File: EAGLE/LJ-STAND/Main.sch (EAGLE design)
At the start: 119 parts

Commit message: TSOP wires routed. Sanity gone.
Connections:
- removed net N$22: SW1.6
- net +3V3: now also BLUETOOTH.2
- net DIP3: now also SW1.6
- net GND: now also BLUETOOTH.3
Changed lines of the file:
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@@
 </segment>
 <segment>
-<wire x1="132.08" y1="182.88" x2="144.78" y2="182.88" width="0.1524" layer="91"/>
 <wire x1="144.78" y1="182.88" x2="144.78" y2="180.34" width="0.1524" layer="91"/>
 <pinref part="GND93" gate="1" pin="GND"/>
+<pinref part="BLUETOOTH" gate="G$1" pin="3"/>
+<wire x1="132.08" y1="182.88" x2="144.78" y2="182.88" width="0.1524" layer="91"/>
 </segment>
 <segment>
@@
 </segment>
 <segment>
-<wire x1="132.08" y1="180.34" x2="134.62" y2="180.34" width="0.1524" layer="91"/>
 <wire x1="134.62" y1="180.34" x2="134.62" y2="175.26" width="0.1524" layer="91"/>
 <wire x1="134.62" y1="175.26" x2="139.7" y2="175.26" width="0.1524" layer="91"/>
 <wire x1="139.7" y1="175.26" x2="139.7" y2="177.8" width="0.1524" layer="91"/>
 <pinref part="+3V21" gate="G$1" pin="+3V3"/>
+<pinref part="BLUETOOTH" gate="G$1" pin="2"/>
+<wire x1="132.08" y1="180.34" x2="134.62" y2="180.34" width="0.1524" layer="91"/>
 </segment>
 <segment>
@@
 </segment>
 </net>
-<net name="N$22" class="0">
-<segment>
-<pinref part="SW1" gate="A" pin="6"/>
-<wire x1="170.18" y1="116.84" x2="195.58" y2="116.84" width="0.1524" layer="91"/>
-</segment>
-</net>
 <net name="DIP2" class="0">
 <segment>
@@
 <net name="DIP3" class="0">
 <segment>
-<wire x1="195.58" y1="116.84" x2="195.58" y2="119.38" width="0.1524" layer="91"/>
-<wire x1="195.58" y1="116.84" x2="200.66" y2="116.84" width="0.1524" layer="91"/>
 <wire x1="200.66" y1="116.84" x2="200.66" y2="132.08" width="0.1524" layer="91"/>
 <label x="200.66" y="132.08" size="1.778" layer="95" rot="R90" xref="yes"/>
+<pinref part="SW1" gate="A" pin="6"/>
+<wire x1="200.66" y1="116.84" x2="195.58" y2="116.84" width="0.1524" layer="91"/>
+<pinref part="R11" gate="G$1" pin="1"/>
+<wire x1="195.58" y1="116.84" x2="170.18" y2="116.84" width="0.1524" layer="91"/>
+<wire x1="195.58" y1="119.38" x2="195.58" y2="116.84" width="0.1524" layer="91"/>
 <junction x="195.58" y="116.84"/>
-<pinref part="R11" gate="G$1" pin="1"/>
-</segment>
-<segment>
+</segment>
+<segment>

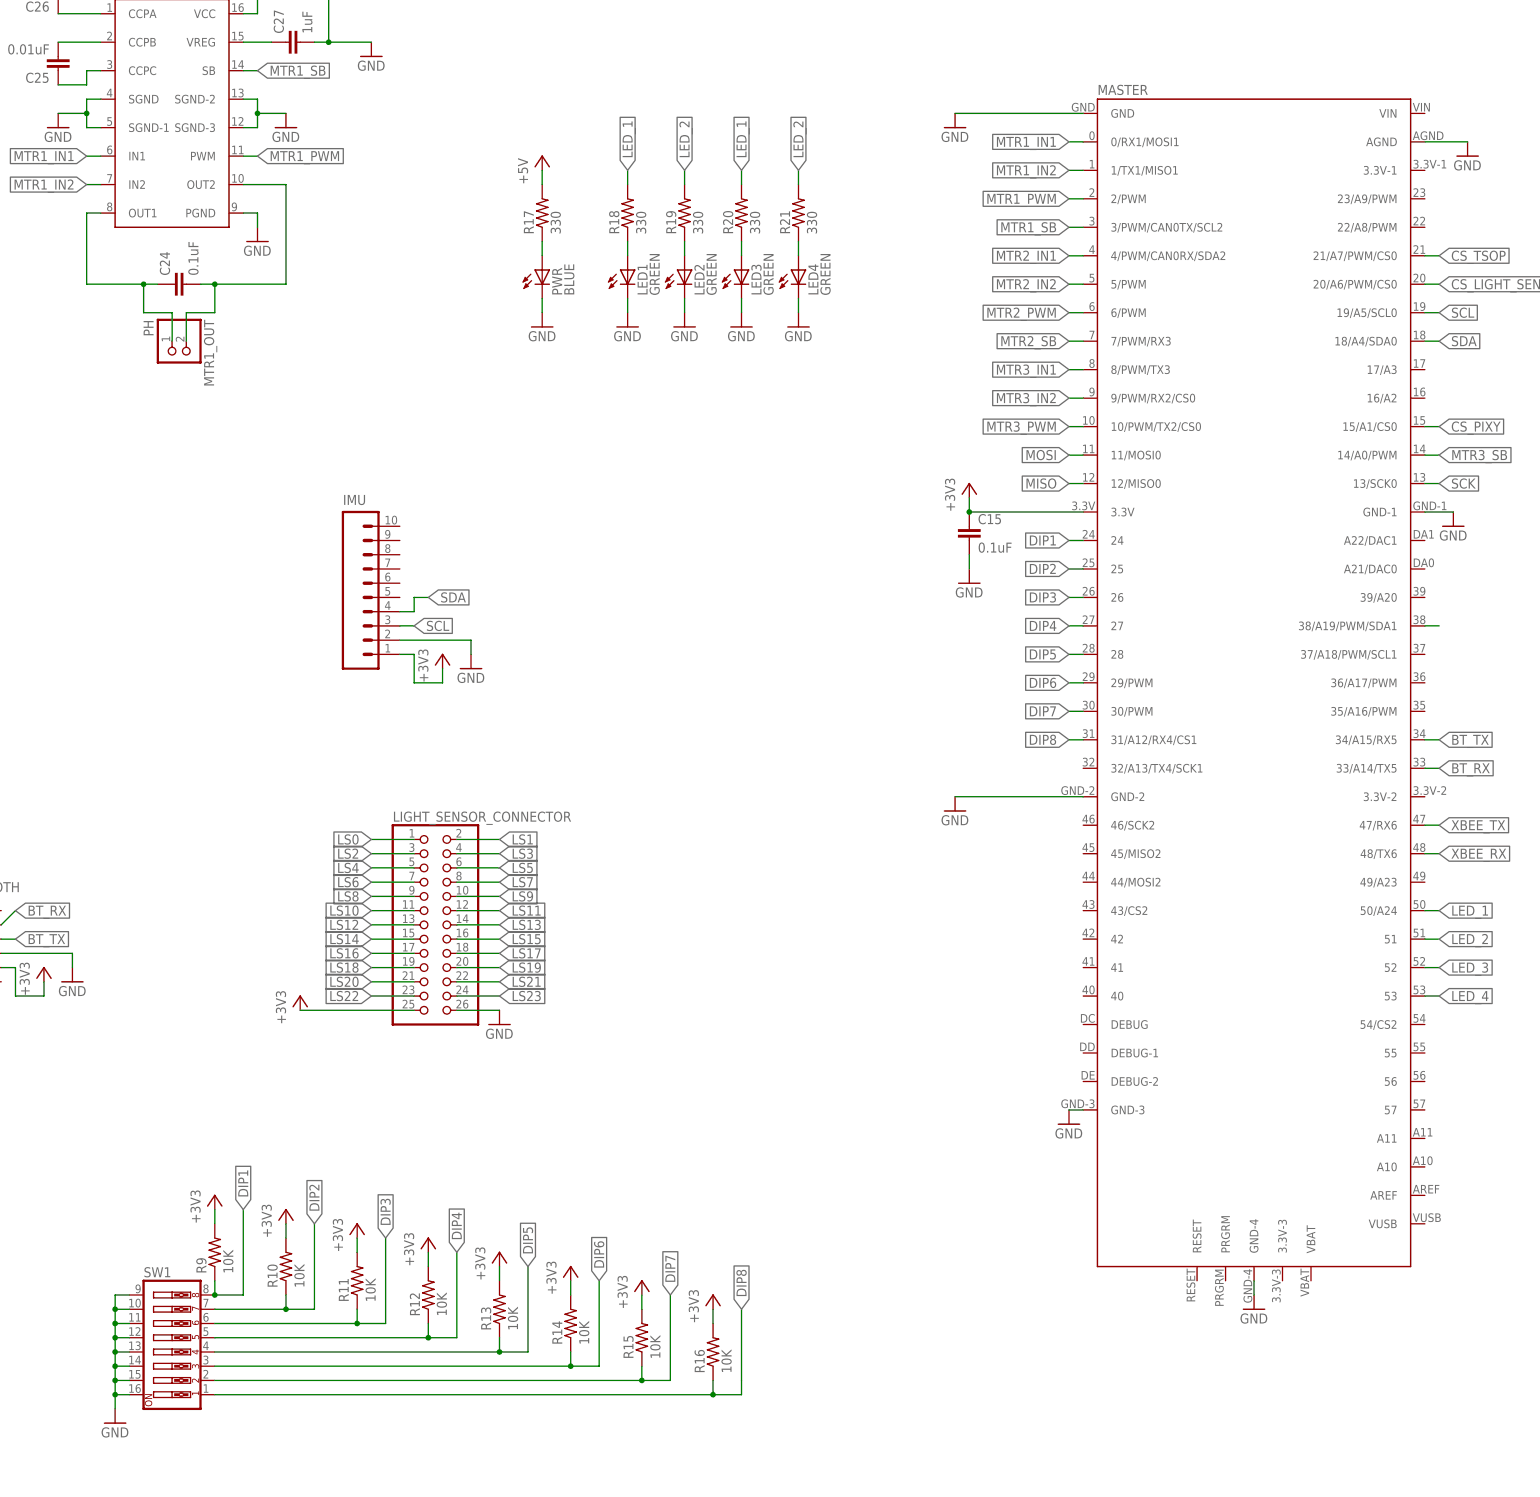
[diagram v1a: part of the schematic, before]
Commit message: Finished main PCB routing
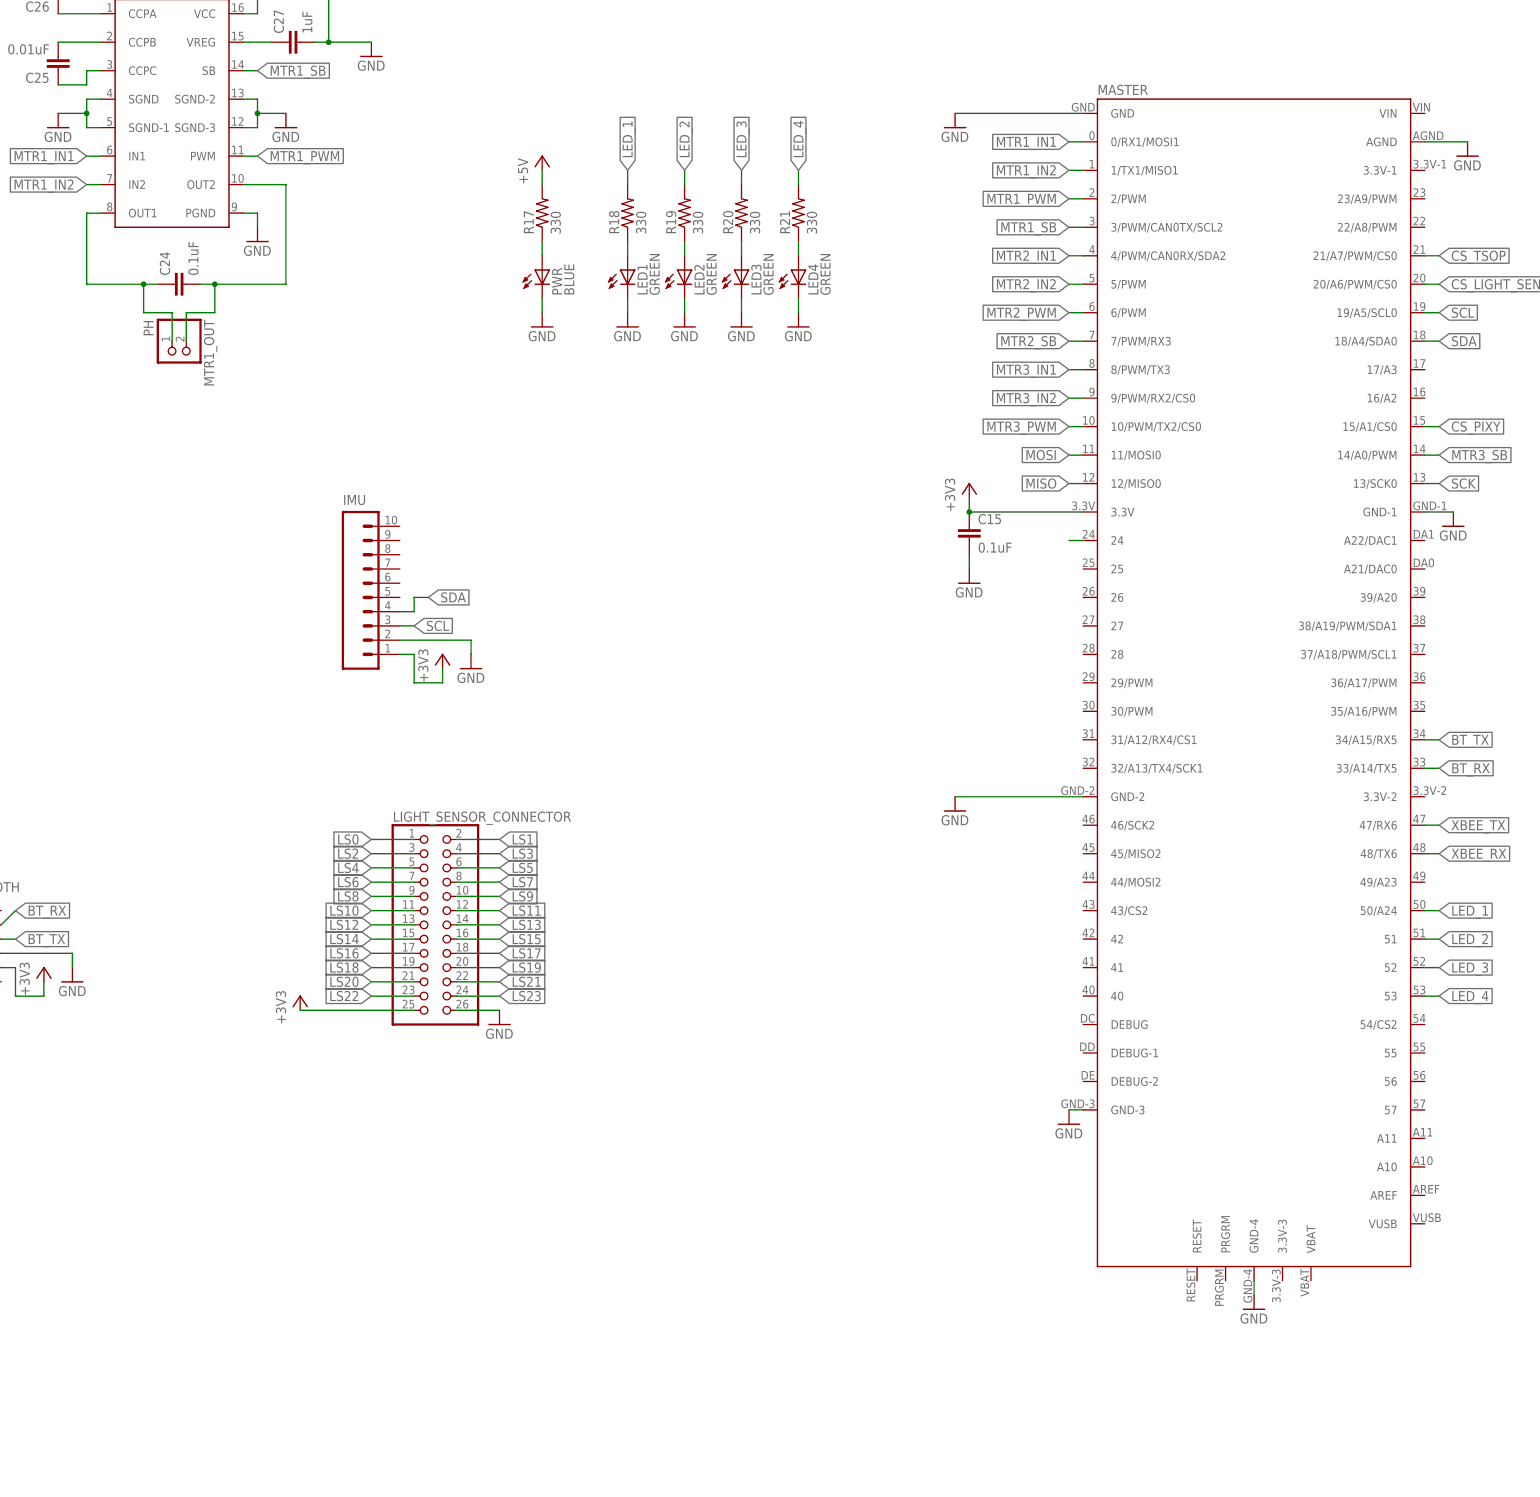
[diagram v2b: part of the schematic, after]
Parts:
- removed R10, R11, R12, R13, R14, R15, R16, R9: 10K, SparkFun-Resistors:RESISTOR0603-RES
- removed SW1: (no value), SparkFun-Electromechanical:SW_DIP-8
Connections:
- removed net DIP2: MASTER.25, R10.1, SW1.7
- removed net DIP3: MASTER.26, R11.1, SW1.6
- removed net DIP4: MASTER.27, R12.1, SW1.5
- removed net DIP5: MASTER.28, R13.1, SW1.4
- removed net DIP6: MASTER.29/PWM, R14.1, SW1.3
- removed net DIP7: MASTER.30/PWM, R15.1, SW1.2
- removed net DIP8: MASTER.31/A12/RX4/CS1, R16.1, SW1.1
- net +3V3: no longer R10.2, R11.2, R12.2, R13.2, R14.2, R15.2, R16.2, R9.2
- net DIP1: no longer R9.1, SW1.8
- net GND: no longer SW1.10, SW1.11, SW1.12, SW1.13, SW1.14, SW1.15, SW1.16, SW1.9
- net LED_1: no longer R20.2
- net LED_2: no longer R21.2
- net LED_3: now also R20.2
- net LED_4: now also R21.2
- net SDA: no longer MASTER.38/A19/PWM/SDA1

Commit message: Teensys
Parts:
- added C48: 100uF, SparkFun-Capacitors:CAP_POLPTH1
- added C49: 0.1uF, SparkFun-Capacitors:CAP0603-CAP
- added C50: 0.01uF, SparkFun-Capacitors:CAP0603-CAP
- added C51: 0.22uF, SparkFun-Capacitors:CAP0603-CAP
- added C52: 1uF, SparkFun-Capacitors:CAP0603-CAP
- added MOTOR_4: TB6549PG, TB6549PG-motor-controller:TB6549PG
- added MTR4_OUT: PH, adafruit:JST_2PIN-SMT
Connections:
- removed net DIP1: MASTER.24
- new net MTR4_IN1: MASTER.17/A3, MOTOR_4.IN1
- new net MTR4_IN2: MASTER.22/A8/PWM, MOTOR_4.IN2
- new net MTR4_PWM: MASTER.23/A9/PWM, MOTOR_4.PWM
- new net MTR4_SB: MASTER.24, MOTOR_4.SB
- new net N$22: C49.1, MOTOR_4.OUT1, MTR4_OUT.2
- new net N$26: C49.2, MOTOR_4.OUT2, MTR4_OUT.1
- new net N$28: C50.2, MOTOR_4.CCPB
- new net N$30: C50.1, MOTOR_4.CCPC
- new net N$31: C51.1, MOTOR_4.CCPA
- new net N$32: C52.1, MOTOR_4.VREG
- net GND: now also C48.-, C51.2, C52.2, MOTOR_4.PGND, MOTOR_4.SGND, MOTOR_4.SGND-1, MOTOR_4.SGND-2, MOTOR_4.SGND-3
- net LED_1: now also MASTER.38/A19/PWM/SDA1; no longer MASTER.50/A24
- net LED_2: now also MASTER.37/A18/PWM/SCL1; no longer MASTER.51
- net LED_3: now also MASTER.36/A17/PWM; no longer MASTER.52
- net LED_4: now also MASTER.35/A16/PWM; no longer MASTER.53
- net MOTOR_PWR: now also C48.+, MOTOR_4.VCC
- net MTR3_SB: now also MASTER.16/A2; no longer MASTER.14/A0/PWM
- net SCK: now also MASTER.14/A0/PWM; no longer MASTER.13/SCK0
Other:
- moved on the sheet: BLUETOOTH, C15, PIXY_I2C, PIXY_SPI, R1, R2, R5, R6, R7, R8, SCL, SDA

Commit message: Light sensor connector
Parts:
- added LED5: WHITE, adafruit:LEDCHIPLED_0603
- added LED6: YELLOW, adafruit:LEDCHIPLED_0603
- added R3, R4: 330, SparkFun-Resistors:RESISTOR0603
- LED2: value GREEN -> ORANGE
- LED3: value GREEN -> PINK
- LED4: value GREEN -> RED
- renumbered MTR1_OUT to MTR1_OUT_RIGHT, MTR2_OUT to MTR2_OUT_LEFT, MTR3_OUT to MTR3_OUT_BACKRIGHT, MTR4_OUT to MTR4_OUT_BACKLEFT
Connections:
- net LED_1 renamed LED1
- net LED_2 renamed LED2
- net LED_3 renamed LED3
- net LED_4 renamed LED4
- removed net CS_LIGHT_SENSOR: MASTER.20/A6/PWM/CS0, SLAVE_LIGHT.10/PWM/TX2/CS0
- new net CS_LIGHT: MASTER.9/PWM/RX2/CS0, SLAVE_LIGHT.10/PWM/TX2/CS0
- new net LED5: MASTER.29/PWM, R3.2
- new net LED6: MASTER.30/PWM, R4.2
- new net N$33: LED5.A, R3.1
- new net N$34: LED6.A, R4.1
- net CS_TSOP: now also MASTER.10/PWM/TX2/CS0, SLAVE_TSOP.10/PWM/TX2/CS0; no longer MASTER.21/A7/PWM/CS0, SLAVE_TSOP.15/A1/CS0
- net GND: now also LED5.C, LED6.C
- net LS0: now also SLAVE_LIGHT.15/A1/CS0; no longer SLAVE_LIGHT.14/A0/PWM
- net LS1: now also SLAVE_LIGHT.16/A2; no longer SLAVE_LIGHT.15/A1/CS0
- net LS10: now also SLAVE_LIGHT.A11; no longer SLAVE_LIGHT.A10
- net LS11: now also SLAVE_LIGHT.31/A12/RX4/CS1; no longer SLAVE_LIGHT.A11
- net LS12: now also SLAVE_LIGHT.32/A13/TX4/SCK1; no longer SLAVE_LIGHT.31/A12/RX4/CS1
- net LS13: now also SLAVE_LIGHT.33/A14/TX5; no longer SLAVE_LIGHT.32/A13/TX4/SCK1
- net LS14: now also SLAVE_LIGHT.34/A15/RX5; no longer SLAVE_LIGHT.33/A14/TX5
- net LS15: now also SLAVE_LIGHT.35/A16/PWM; no longer SLAVE_LIGHT.34/A15/RX5
- net LS16: now also SLAVE_LIGHT.36/A17/PWM; no longer SLAVE_LIGHT.35/A16/PWM
- net LS17: now also SLAVE_LIGHT.37/A18/PWM/SCL1; no longer SLAVE_LIGHT.36/A17/PWM
- net LS18: now also SLAVE_LIGHT.38/A19/PWM/SDA1; no longer SLAVE_LIGHT.37/A18/PWM/SCL1
- net LS19: now also SLAVE_LIGHT.39/A20; no longer SLAVE_LIGHT.38/A19/PWM/SDA1
- net LS2: now also SLAVE_LIGHT.17/A3; no longer SLAVE_LIGHT.16/A2
- net LS20: now also SLAVE_LIGHT.A21/DAC0; no longer SLAVE_LIGHT.39/A20
- net LS21: now also SLAVE_LIGHT.A22/DAC1; no longer SLAVE_LIGHT.A21/DAC0
- net LS22: now also SLAVE_LIGHT.49/A23; no longer SLAVE_LIGHT.A22/DAC1
- net LS23: now also SLAVE_LIGHT.50/A24; no longer SLAVE_LIGHT.49/A23
- net LS3: now also SLAVE_LIGHT.18/A4/SDA0; no longer SLAVE_LIGHT.17/A3
- net LS4: now also SLAVE_LIGHT.19/A5/SCL0; no longer SLAVE_LIGHT.18/A4/SDA0
- net LS5: now also SLAVE_LIGHT.20/A6/PWM/CS0; no longer SLAVE_LIGHT.19/A5/SCL0
- net LS6: now also SLAVE_LIGHT.21/A7/PWM/CS0; no longer SLAVE_LIGHT.20/A6/PWM/CS0
- net LS7: now also SLAVE_LIGHT.22/A8/PWM; no longer SLAVE_LIGHT.21/A7/PWM/CS0
- net LS8: now also SLAVE_LIGHT.23/A9/PWM; no longer SLAVE_LIGHT.22/A8/PWM
- net LS9: now also SLAVE_LIGHT.A10; no longer SLAVE_LIGHT.23/A9/PWM
- net MISO: now also SLAVE_LIGHT.11/MOSI0, SLAVE_TSOP.11/MOSI0; no longer SLAVE_LIGHT.12/MISO0, SLAVE_TSOP.12/MISO0
- net MOSI: now also SLAVE_LIGHT.12/MISO0, SLAVE_TSOP.12/MISO0; no longer SLAVE_LIGHT.11/MOSI0, SLAVE_TSOP.11/MOSI0
- net MTR3_IN2: now also MASTER.16/A2; no longer MASTER.9/PWM/RX2/CS0
- net MTR3_PWM: now also MASTER.20/A6/PWM/CS0; no longer MASTER.10/PWM/TX2/CS0
- net MTR3_SB: now also MASTER.17/A3; no longer MASTER.16/A2
- net MTR4_IN1: now also MASTER.21/A7/PWM/CS0; no longer MASTER.17/A3
- net SCK: now also SLAVE_LIGHT.14/A0/PWM, SLAVE_TSOP.14/A0/PWM; no longer SLAVE_LIGHT.13/SCK0, SLAVE_TSOP.13/SCK0
- net TSOP10: now also SLAVE_TSOP.15/A1/CS0; no longer SLAVE_TSOP.10/PWM/TX2/CS0
- net TSOP11: now also SLAVE_TSOP.16/A2; no longer SLAVE_TSOP.14/A0/PWM
- net TSOP12: now also SLAVE_TSOP.17/A3; no longer SLAVE_TSOP.16/A2
- net TSOP13: now also SLAVE_TSOP.18/A4/SDA0; no longer SLAVE_TSOP.17/A3
- net TSOP14: now also SLAVE_TSOP.19/A5/SCL0; no longer SLAVE_TSOP.18/A4/SDA0
- net TSOP15: now also SLAVE_TSOP.20/A6/PWM/CS0; no longer SLAVE_TSOP.19/A5/SCL0
- net TSOP16: now also SLAVE_TSOP.21/A7/PWM/CS0; no longer SLAVE_TSOP.20/A6/PWM/CS0
- net TSOP17: now also SLAVE_TSOP.22/A8/PWM; no longer SLAVE_TSOP.21/A7/PWM/CS0
- net TSOP18: now also SLAVE_TSOP.23/A9/PWM; no longer SLAVE_TSOP.22/A8/PWM
- net TSOP19: now also SLAVE_TSOP.24; no longer SLAVE_TSOP.23/A9/PWM
- net TSOP20: now also SLAVE_TSOP.25; no longer SLAVE_TSOP.24
- net TSOP21: now also SLAVE_TSOP.26; no longer SLAVE_TSOP.25
- net TSOP22: now also SLAVE_TSOP.27; no longer SLAVE_TSOP.26
- net TSOP23: now also SLAVE_TSOP.28; no longer SLAVE_TSOP.27
- net TSOP_PWR: now also SLAVE_TSOP.32/A13/TX4/SCK1; no longer SLAVE_TSOP.28
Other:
- moved on the sheet: LED1, LED2, LED3, LED4, PWR, R17, R18, R19, R20, R21
